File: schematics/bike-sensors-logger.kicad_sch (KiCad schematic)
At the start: 3 parts, among them J1 MMCX, U1 RaspberryPi_Zero_Dummy

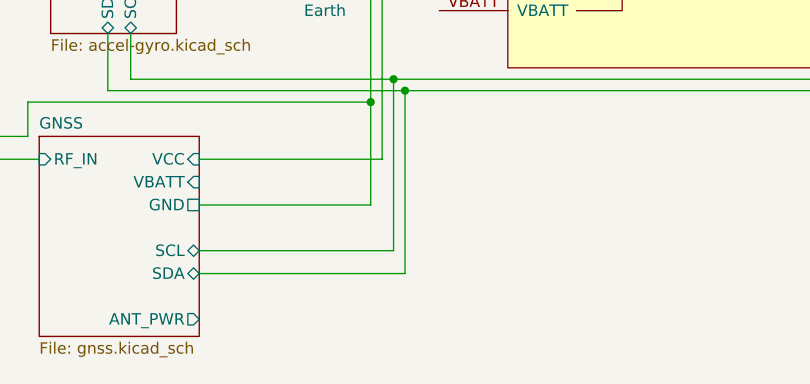
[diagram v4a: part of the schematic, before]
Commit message: Added GNSS powered antenna witch LED
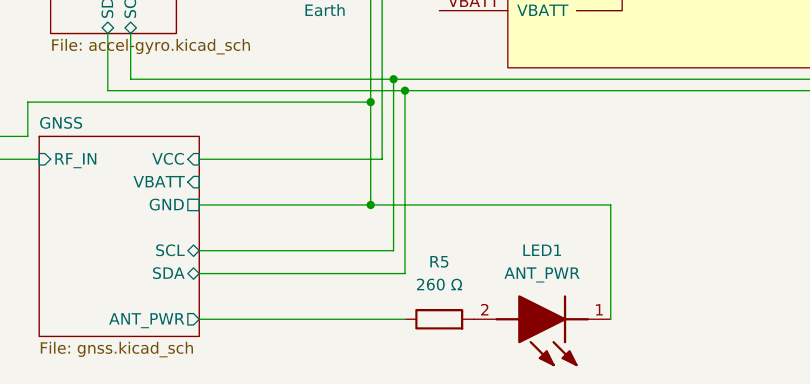
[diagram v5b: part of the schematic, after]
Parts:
- added LED1: ANT_PWR, LEDC1608X115N, symbol 150060RS83000:150060RS83000
- added R5: 260 Ω, symbol Device:R
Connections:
- net Earth: now also LED1.1 (K)
- net GNSS/ANT_PWR: now also R5.1
- new net: LED1.2 (A), R5.2
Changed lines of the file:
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@@
+	)
+	(junction
+		(at 80.01 99.06)
+		(diameter 0)
+		(color 0 0 0 0)
 	)
 	(junction
@@
 	(wire
 		(pts
+			(xy 60.96 111.76) (xy 83.82 111.76)
+		)
+		(stroke
+			(width 0)
+			(type default)
+		)
+	)
+	(wire
+		(pts
 			(xy 81.28 41.91) (xy 81.28 64.77)
 		)
@@
 	(wire
 		(pts
+			(xy 106.68 111.76) (xy 106.68 99.06)
+		)
+		(stroke
+			(width 0)
+			(type default)
+		)
+	)
+	(wire
+		(pts
+			(xy 80.01 99.06) (xy 106.68 99.06)
+		)
+		(stroke
+			(width 0)
+			(type default)
+		)
+	)
+	(wire
+		(pts
 			(xy 80.01 72.39) (xy 80.01 87.63)
 		)
@@
 			(width 0)
 			(type default)
+		)
+	)
+	(symbol
+		(lib_id "150060RS83000:150060RS83000")
+		(at 106.68 111.76 180)
+		(unit 1)
+		(exclude_from_sim no)
+		(in_bom yes)
+		(on_board yes)
+		(dnp no)
+		(fields_autoplaced yes)
+		(property "Reference" "LED1"
+			(at 99.06 104.14 0)
+			(effects
+				(font
+					(size 1.27 1.27)
+				)
+			)
+		)
+		(property "Value" "ANT_PWR"
+			(at 99.06 106.68 0)
+			(effects
+				(font
+					(size 1.27 1.27)
+				)
+			)
+		)
+		(property "Footprint" "LEDC1608X115N"
+			(at 93.98 18.11 0)
+			(effects
+				(font
+					(size 1.27 1.27)
+				)
+				(justify left bottom)
+				(hide yes)
+			)
+		)
+		(property "Datasheet" ""
+			(at 93.98 -81.89 0)
+			(effects
+				(font
+					(size 1.27 1.27)
+				)
+				(justify left bottom)
+				(hide yes)
+			)
+		)
+		(property "Description" "Red 625nm LED Indication - Discrete 2V 0603 (1608 Metric)"
+			(at 106.68 111.76 0)
+			(effects
+				(font
+					(size 1.27 1.27)
+				)
+				(hide yes)
+			)
+		)
+		(property "Height" "1.15"
+			(at 93.98 -281.89 0)
+			(effects
+				(font
+					(size 1.27 1.27)
+				)
+				(justify left bottom)
+				(hide yes)
+			)
+		)
+		(property "Mouser Part Number" ""
+			(at 93.98 -381.89 0)
+			(effects
+				(font
+					(size 1.27 1.27)
+				)
+				(justify left bottom)
+				(hide yes)
+			)
+		)
+		(property "Mouser Price/Stock" ""
+			(at 93.98 -481.89 0)
+			(effects
+				(font
+					(size 1.27 1.27)
+				)
+				(justify left bottom)
+				(hide yes)
+			)
+		)
+		(property "Manufacturer_Name" "Wurth Elektronik"
+			(at 93.98 -581.89 0)
+			(effects
+				(font
+					(size 1.27 1.27)
+				)
+				(justify left bottom)
+				(hide yes)
+			)
+		)
+		(property "Manufacturer_Part_Number" "150060RS83000"
+			(at 93.98 -681.89 0)
+			(effects
+				(font
+					(size 1.27 1.27)
+				)
+				(justify left bottom)
+				(hide yes)
+			)
+		)
+		(pin "1"
+		)
+		(pin "2"
+		)
+		(instances
+			(project ""
+				(path "/2c1d9222-af16-428b-85a5-a3d420373d70"
+					(reference "LED1")
+					(unit 1)
+				)
+			)
 		)
 	)
@@
 					(unit 1)
 				)
+			)
+		)
+	)
+	(symbol
+		(lib_id "Device:R")
+		(at 87.63 111.76 90)
+		(unit 1)
+		(exclude_from_sim no)
+		(in_bom yes)
+		(on_board yes)
+		(dnp no)
+		(fields_autoplaced yes)
+		(property "Reference" "R5"
+			(at 87.63 105.41 90)
+			(effects
+				(font
+					(size 1.27 1.27)
+				)
+			)
+		)
+		(property "Value" "260 Ω"
+			(at 87.63 107.95 90)
+			(effects
+				(font
+					(size 1.27 1.27)
+				)
+			)
+		)
+		(property "Footprint" ""
+			(at 87.63 113.538 90)
+			(effects
+				(font
+					(size 1.27 1.27)
+				)
+				(hide yes)
+			)
+		)
+		(property "Datasheet" "~"
+			(at 87.63 111.76 0)
+			(effects
+				(font
+					(size 1.27 1.27)
+				)
+				(hide yes)
+			)
+		)
+		(property "Description" "Resistor"
+			(at 87.63 111.76 0)
+			(effects
+				(font
+					(size 1.27 1.27)
+				)
+				(hide yes)
+			)
+		)
+		(pin "2"
+		)
+		(pin "1"
+		)
+		(instances
+			(project ""
+				(path "/2c1d9222-af16-428b-85a5-a3d420373d70"
+					(reference "R5")
+					(unit 1)
+				)

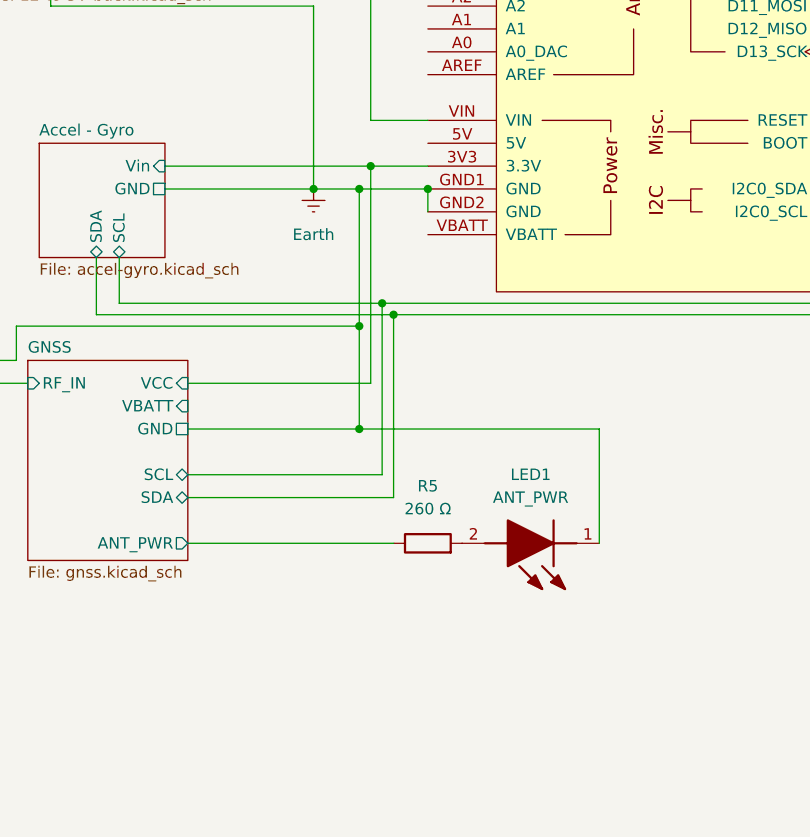
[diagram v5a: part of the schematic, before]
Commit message: Added general power led indicator
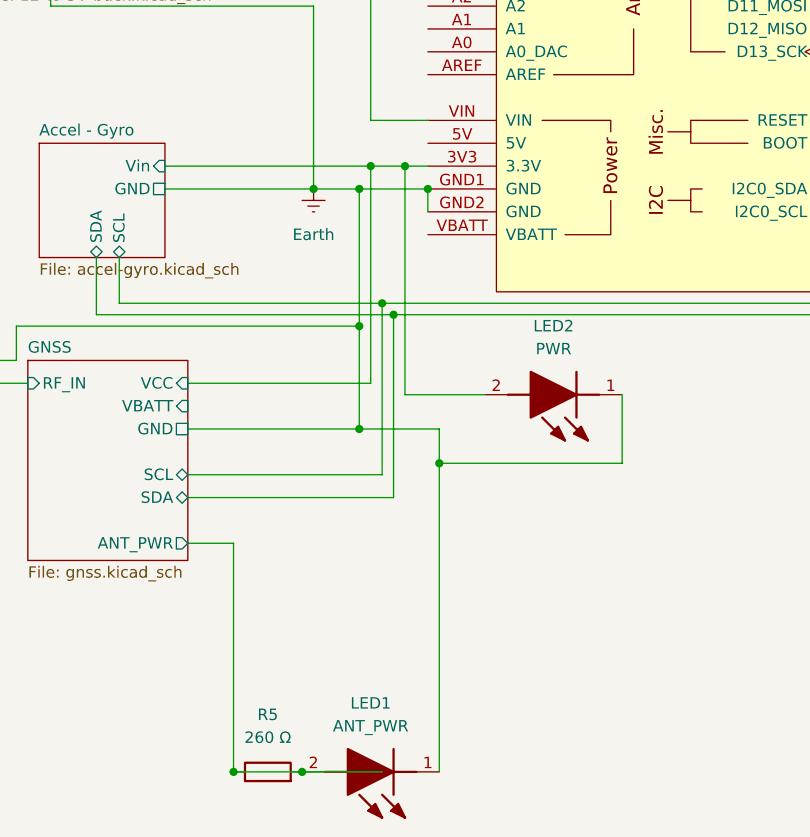
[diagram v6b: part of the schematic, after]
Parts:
- added LED2: PWR, LEDC1608X115N, symbol 150060RS83000:150060RS83000
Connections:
- net Accel - Gyro/Vin: now also LED2.2 (A)
- net Earth: now also LED2.1 (K)
- net GNSS/ANT_PWR: now also LED1.2 (A), R5.2
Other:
- moved on the sheet: LED1, R5

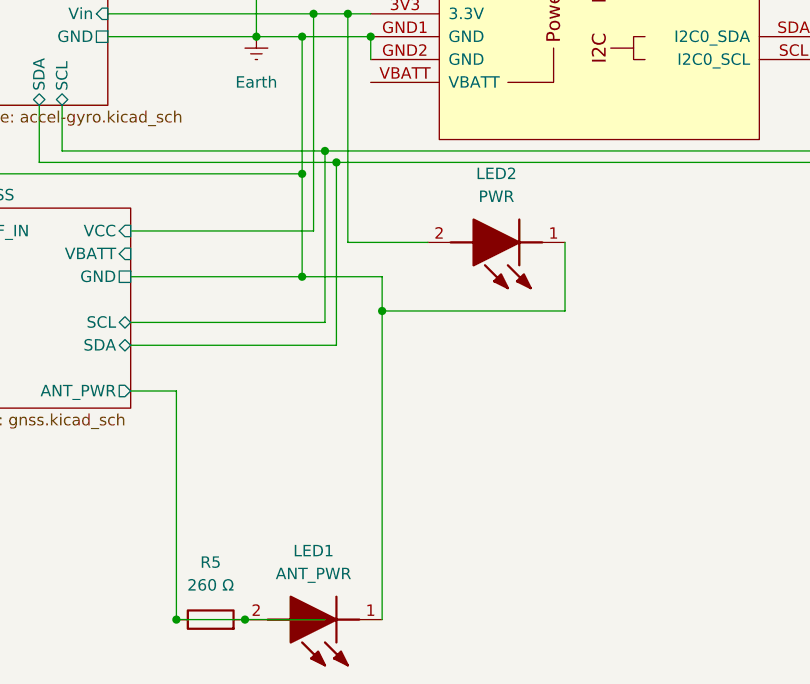
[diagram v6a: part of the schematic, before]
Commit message: Reordered LEDs
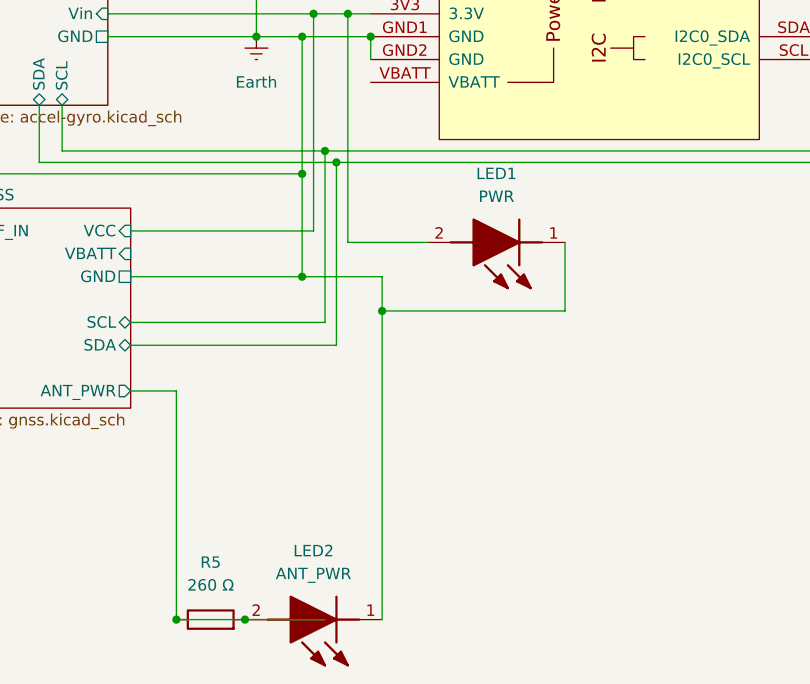
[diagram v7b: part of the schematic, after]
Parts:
- renumbered LED2 to LED1, LED1 to LED2
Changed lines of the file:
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@@
 		(dnp no)
 		(fields_autoplaced yes)
-		(property "Reference" "LED2"
+		(property "Reference" "LED1"
 			(at 101.6 87.63 0)
 			(effects
@@
 			(project "bike-sensors-logger"
 				(path "/2c1d9222-af16-428b-85a5-a3d420373d70"
-					(reference "LED2")
+					(reference "LED1")
 					(unit 1)
 				)
@@
 		(dnp no)
 		(fields_autoplaced yes)
-		(property "Reference" "LED1"
+		(property "Reference" "LED2"
 			(at 81.28 129.54 0)
 			(effects
@@
 			(project ""
 				(path "/2c1d9222-af16-428b-85a5-a3d420373d70"
-					(reference "LED1")
+					(reference "LED2")
 					(unit 1)
 				)

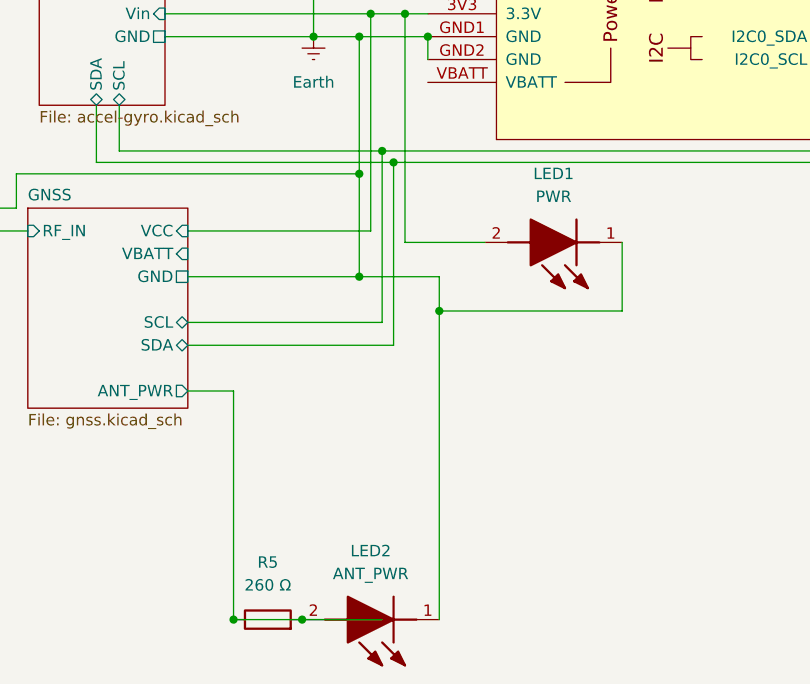
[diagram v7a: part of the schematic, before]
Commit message: Fix wiring typos; Added missing LED1 resistor
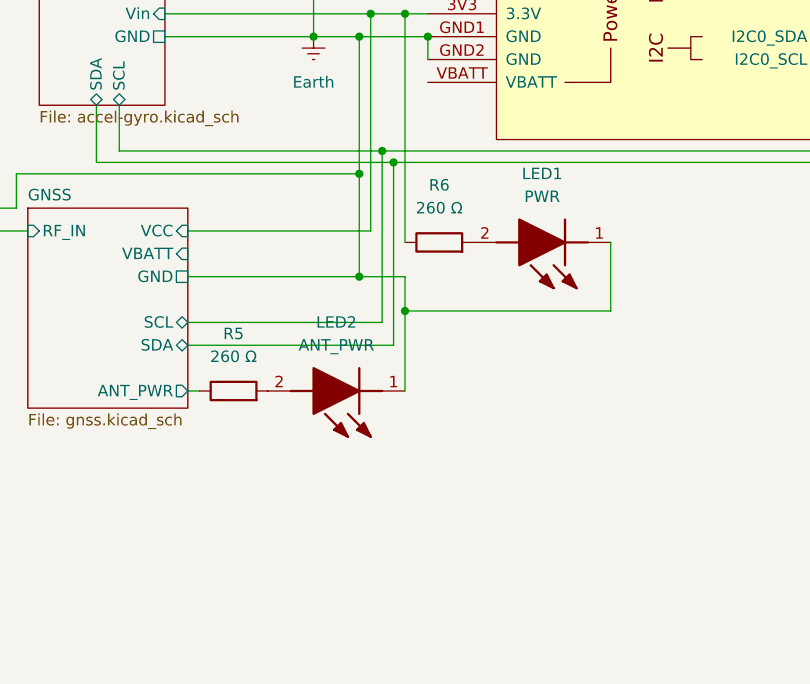
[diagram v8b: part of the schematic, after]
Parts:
- added R6: 260 Ω, symbol Device:R
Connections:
- net Accel - Gyro/Vin: now also R6.1; no longer LED1.2 (A)
- net GNSS/ANT_PWR: no longer LED2.2 (A), R5.2
- new net: LED1.2 (A), R6.2
- new net: LED2.2 (A), R5.2
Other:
- moved on the sheet: LED1, LED2, R5
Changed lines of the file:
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@@
-	)
-	(junction
-		(at 73.66 137.16)
-		(diameter 0)
-		(color 0 0 0 0)
 	)
 	(junction
@@
 	)
 	(junction
-		(at 88.9 102.87)
+		(at 85.09 102.87)
 		(diameter 0)
 		(color 0 0 0 0)
@@
 	)
 	(junction
-		(at 66.04 137.16)
-		(diameter 0)
-		(color 0 0 0 0)
-	)
-	(junction
 		(at 83.82 86.36)
 		(diameter 0)
@@
 	(wire
 		(pts
-			(xy 82.55 137.16) (xy 73.66 137.16)
-		)
-		(stroke
-			(width 0)
-			(type default)
-		)
-	)
-	(wire
-		(pts
 			(xy 81.28 41.91) (xy 81.28 64.77)
 		)
@@
 	(wire
 		(pts
-			(xy 60.96 111.76) (xy 66.04 111.76)
+			(xy 60.96 111.76) (xy 62.23 111.76)
 		)
 		(stroke
@@
 	(wire
 		(pts
-			(xy 88.9 102.87) (xy 88.9 99.06)
+			(xy 85.09 102.87) (xy 85.09 99.06)
 		)
 		(stroke
@@
 	(wire
 		(pts
-			(xy 88.9 102.87) (xy 109.22 102.87)
+			(xy 85.09 102.87) (xy 107.95 102.87)
 		)
 		(stroke
@@
 	(wire
 		(pts
-			(xy 93.98 95.25) (xy 85.09 95.25)
-		)
-		(stroke
-			(width 0)
-			(type default)
-		)
-	)
-	(wire
-		(pts
 			(xy 82.55 85.09) (xy 138.43 85.09)
 		)
@@
 	(wire
 		(pts
-			(xy 88.9 137.16) (xy 88.9 102.87)
-		)
-		(stroke
-			(width 0)
-			(type default)
-		)
-	)
-	(wire
-		(pts
-			(xy 73.66 137.16) (xy 66.04 137.16)
-		)
-		(stroke
-			(width 0)
-			(type default)
-		)
-	)
-	(wire
-		(pts
-			(xy 80.01 99.06) (xy 88.9 99.06)
+			(xy 85.09 111.76) (xy 85.09 102.87)
+		)
+		(stroke
+			(width 0)
+			(type default)
+		)
+	)
+	(wire
+		(pts
+			(xy 80.01 99.06) (xy 85.09 99.06)
 		)
 		(stroke
@@
 	(wire
 		(pts
-			(xy 66.04 111.76) (xy 66.04 137.16)
-		)
-		(stroke
-			(width 0)
-			(type default)
-		)
-	)
-	(wire
-		(pts
 			(xy 60.96 104.14) (xy 82.55 104.14)
 		)
@@
 	(wire
 		(pts
-			(xy 109.22 95.25) (xy 109.22 102.87)
+			(xy 107.95 95.25) (xy 107.95 102.87)
 		)
 		(stroke
@@
 	(symbol
 		(lib_id "150060RS83000:150060RS83000")
-		(at 109.22 95.25 180)
+		(at 107.95 95.25 180)
 		(unit 1)
 		(exclude_from_sim no)
@@
 		(fields_autoplaced yes)
 		(property "Reference" "LED1"
-			(at 101.6 87.63 0)
+			(at 100.33 87.63 0)
 			(effects
 				(font
@@
 		)
 		(property "Value" "PWR"
-			(at 101.6 90.17 0)
+			(at 100.33 90.17 0)
 			(effects
 				(font
@@
 		)
 		(property "Footprint" "LEDC1608X115N"
-			(at 96.52 1.6 0)
+			(at 95.25 1.6 0)
 			(effects
 				(font
@@
 		)
 		(property "Datasheet" ""
-			(at 96.52 -98.4 0)
+			(at 95.25 -98.4 0)
 			(effects
 				(font
@@
 		)
 		(property "Description" "Red 625nm LED Indication - Discrete 2V 0603 (1608 Metric)"
-			(at 109.22 95.25 0)
+			(at 107.95 95.25 0)
 			(effects
 				(font
@@
 		)
 		(property "Height" "1.15"
-			(at 96.52 -298.4 0)
+			(at 95.25 -298.4 0)
 			(effects
 				(font
@@
 		)
 		(property "Mouser Part Number" ""
-			(at 96.52 -398.4 0)
+			(at 95.25 -398.4 0)
 			(effects
 				(font
@@
 		)
 		(property "Mouser Price/Stock" ""
-			(at 96.52 -498.4 0)
+			(at 95.25 -498.4 0)
 			(effects
 				(font
@@
 		)
 		(property "Manufacturer_Name" "Wurth Elektronik"
-			(at 96.52 -598.4 0)
+			(at 95.25 -598.4 0)
 			(effects
 				(font
@@
 		)
 		(property "Manufacturer_Part_Number" "150060RS83000"
-			(at 96.52 -698.4 0)
+			(at 95.25 -698.4 0)
 			(effects
 				(font
@@
 	(symbol
 		(lib_id "150060RS83000:150060RS83000")
-		(at 88.9 137.16 180)
+		(at 85.09 111.76 180)
 		(unit 1)
 		(exclude_from_sim no)
@@
 		(fields_autoplaced yes)
 		(property "Reference" "LED2"
-			(at 81.28 129.54 0)
+			(at 77.47 104.14 0)
 			(effects
 				(font
@@
 		)
 		(property "Value" "ANT_PWR"
-			(at 81.28 132.08 0)
+			(at 77.47 106.68 0)
 			(effects
 				(font
@@
 		)
 		(property "Footprint" "LEDC1608X115N"
-			(at 76.2 43.51 0)
+			(at 72.39 18.11 0)
 			(effects
 				(font
@@
 		)
 		(property "Datasheet" ""
-			(at 76.2 -56.49 0)
+			(at 72.39 -81.89 0)
 			(effects
 				(font
@@
 		)
 		(property "Description" "Red 625nm LED Indication - Discrete 2V 0603 (1608 Metric)"
-			(at 88.9 137.16 0)
+			(at 85.09 111.76 0)
 			(effects
 				(font
@@
 		)
 		(property "Height" "1.15"
-			(at 76.2 -256.49 0)
+			(at 72.39 -281.89 0)
 			(effects
 				(font
@@
 		)
 		(property "Mouser Part Number" ""
-			(at 76.2 -356.49 0)
+			(at 72.39 -381.89 0)
 			(effects
 				(font
@@
 		)
 		(property "Mouser Price/Stock" ""
-			(at 76.2 -456.49 0)
+			(at 72.39 -481.89 0)
 			(effects
 				(font
@@
 		)
 		(property "Manufacturer_Name" "Wurth Elektronik"
-			(at 76.2 -556.49 0)
+			(at 72.39 -581.89 0)
 			(effects
 				(font
@@
 		)
 		(property "Manufacturer_Part_Number" "150060RS83000"
-			(at 76.2 -656.49 0)
+			(at 72.39 -681.89 0)
 			(effects
 				(font
@@
 	(symbol
 		(lib_id "Device:R")
-		(at 69.85 137.16 90)
+		(at 66.04 111.76 90)
 		(unit 1)
 		(exclude_from_sim no)
@@
 		(fields_autoplaced yes)
 		(property "Reference" "R5"
-			(at 69.85 130.81 90)
+			(at 66.04 105.41 90)
 			(effects
 				(font
@@
 		)
 		(property "Value" "260 Ω"
-			(at 69.85 133.35 90)
+			(at 66.04 107.95 90)
 			(effects
 				(font
@@
 		)
 		(property "Footprint" ""
-			(at 69.85 138.938 90)
+			(at 66.04 113.538 90)
 			(effects
 				(font
@@
 		)
 		(property "Datasheet" "~"
-			(at 69.85 137.16 0)
+			(at 66.04 111.76 0)
 			(effects
 				(font
@@
 		)
 		(property "Description" "Resistor"
-			(at 69.85 137.16 0)
+			(at 66.04 111.76 0)
 			(effects
 				(font
@@
 					(unit 1)
 				)
+			)
+		)
+	)
+	(symbol
+		(lib_id "Device:R")
+		(at 88.9 95.25 90)
+		(unit 1)
+		(exclude_from_sim no)
+		(in_bom yes)
+		(on_board yes)
+		(dnp no)
+		(fields_autoplaced yes)
+		(property "Reference" "R6"
+			(at 88.9 88.9 90)
+			(effects
+				(font
+					(size 1.27 1.27)
+				)
+			)
+		)
+		(property "Value" "260 Ω"
+			(at 88.9 91.44 90)
+			(effects
+				(font
+					(size 1.27 1.27)
+				)
+			)
+		)
+		(property "Footprint" ""
+			(at 88.9 97.028 90)
+			(effects
+				(font
+					(size 1.27 1.27)
+				)
+				(hide yes)
+			)
+		)
+		(property "Datasheet" "~"
+			(at 88.9 95.25 0)
+			(effects
+				(font
+					(size 1.27 1.27)
+				)
+				(hide yes)
+			)
+		)
+		(property "Description" "Resistor"
+			(at 88.9 95.25 0)
+			(effects
+				(font
+					(size 1.27 1.27)
+				)
+				(hide yes)
+			)
+		)
+		(pin "2"
+		)
+		(pin "1"
+		)
+		(instances
+			(project "bike-sensors-logger"
+				(path "/2c1d9222-af16-428b-85a5-a3d420373d70"
+					(reference "R6")
+					(unit 1)
+				)
